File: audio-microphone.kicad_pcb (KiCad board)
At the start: 2 copper layers, 11.2 x 11.5 mm, 9 parts, among them J1 JST_SUR_1x5_BM05B-SURS-TB-LF-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

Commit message: [#71550] Change PCB to 4 layers
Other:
- copper layers 2 -> 4
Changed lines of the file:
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@@
 	(layers
 		(0 "F.Cu" signal)
+		(1 "In1.Cu" signal)
+		(2 "In2.Cu" signal)
 		(31 "B.Cu" signal)
 		(32 "B.Adhes" user "B.Adhesive")
@@
 			)
 			(layer "dielectric 1"
-				(type "core")
+				(type "prepreg")
 				(color "Polyimide")
-				(thickness 1.51)
+				(thickness 0.1)
 				(material "FR4")
 				(epsilon_r 4.5)
+				(loss_tangent 0.02)
+			)
+			(layer "In1.Cu"
+				(type "copper")
+				(thickness 0.035)
+			)
+			(layer "dielectric 2"
+				(type "core")
+				(thickness 1.24)
+				(material "FR4")
+				(epsilon_r 4.5)
+				(loss_tangent 0.02)
+			)
+			(layer "In2.Cu"
+				(type "copper")
+				(thickness 0.035)
+			)
+			(layer "dielectric 3"
+				(type "prepreg")
+				(thickness 0.1)
+				(material "FR4")
+				(epsilon_r 4.5)

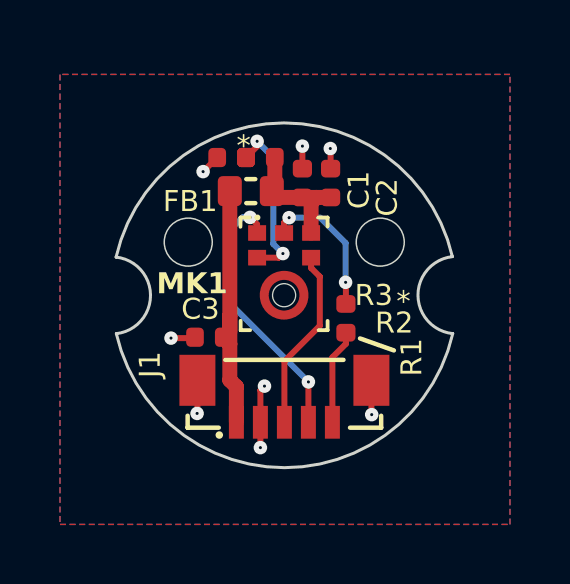
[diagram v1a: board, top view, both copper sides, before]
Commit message: [#71550] Change FB1 to 0402 size one BLM15AG601SN1D
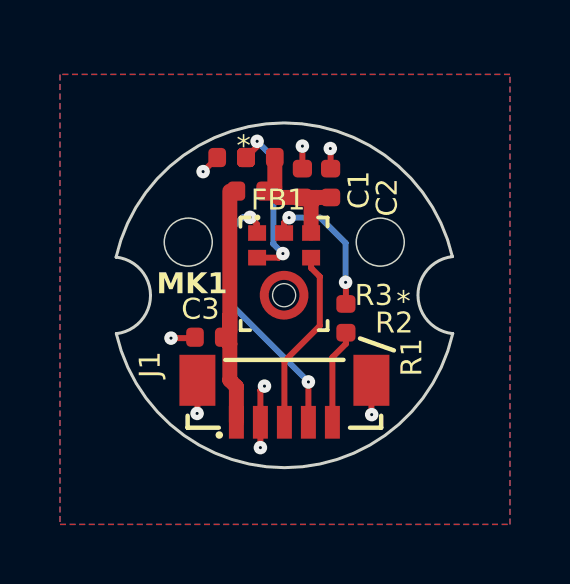
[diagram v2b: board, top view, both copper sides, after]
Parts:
- FB1: value FB_600Z_0.5A_Murata-BLM18AG_0603 -> FB_600Z_0.3A_Murata-BLM15AG_0402; footprint antmicro-footprints:FB_0603_1608Metric -> antmicro-footprints:FB_0402_1005Metric

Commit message: [#71550] Re-arrange components, finish routing
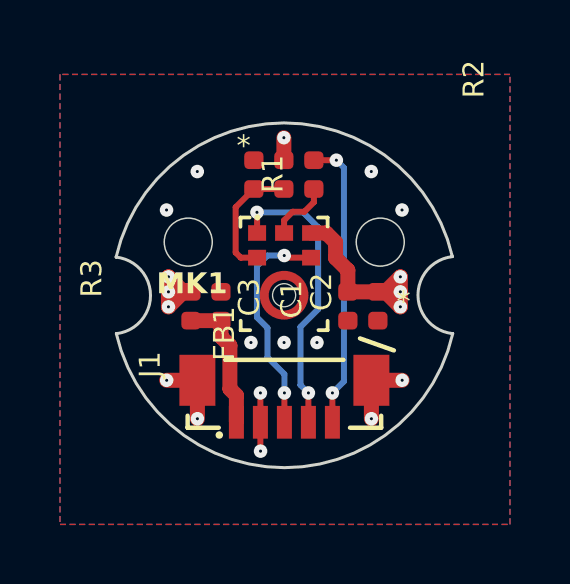
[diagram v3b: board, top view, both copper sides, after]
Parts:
- moved R1 4.91 mm to (241.0, 142.9), turned to 90 degrees
- moved C2 4.40 mm to (243.1, 147.3), turned to -90 degrees
- moved C1 4.38 mm to (242.1, 147.3), turned to 90 degrees
- moved FB1 4.32 mm to (236.9, 147.3), turned to -90 degrees
- moved C3 1.10 mm to (237.9, 147.3), turned to -90 degrees
- moved R2 0.97 mm to (240.0, 142.9), turned to 90 degrees
- moved R3 0.94 mm to (239.0, 142.9), turned to -90 degrees
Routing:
- net VDD: track 4.47 -> 11.3 mm, vias 0 -> 7
- net /DATA: track 3.17 -> 9.75 mm, vias 0 -> 2
- net VCC: track 8.62 -> 4.60 mm
- net Net-(MK1-DATA): track 4.85 -> 2.11 mm, vias 2 -> 0
- net /SELECT: track 5.71 -> 4.16 mm, vias 2 -> 0
- net /BCLK: track 6.10 -> 7.57 mm, vias 0 -> 2
- net /WS: track 9.00 -> 9.79 mm
- net GND: track 7.25 -> 6.56 mm, vias 8 -> 13
- added copper zone on In1.Cu, net GND
- added copper zone on In2.Cu, net VDD

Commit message: [#71550] Remove unnecessary vias
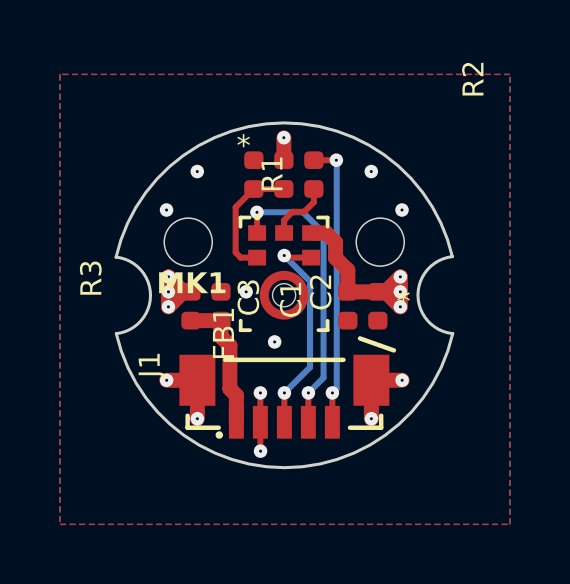
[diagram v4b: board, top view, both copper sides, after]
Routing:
- net GND: vias 13 -> 12
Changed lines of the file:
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@@
 	)
 	(via
-		(at 239.97 148.497305)
+		(at 239.655108 148.477305)
 		(size 0.45)
 		(drill 0.1)
@@
 	)
 	(via
-		(at 241.065108 148.497305)
-		(size 0.45)
-		(drill 0.1)
-		(layers "F.Cu" "B.Cu")
-		(net 2)
-	)
-	(via
 		(at 237.08 151.037305)
 		(size 0.45)
@@
 	)
 	(via
-		(at 238.865108 148.497305)
-		(size 0.45)
-		(drill 0.1)
-		(layers "F.Cu" "B.Cu")
-		(net 2)
-	)
-	(via
 		(at 242.876194 142.79752)
+		(size 0.45)
+		(drill 0.1)
+		(layers "F.Cu" "B.Cu")
+		(net 2)
+	)
+	(via
+		(at 238.705108 146.807305)
 		(size 0.45)
 		(drill 0.1)
@@
 	)
 	(segment
+		(start 241.285108 144.837305)
+		(end 241.285108 149.672197)
+		(width 0.2)
+		(layer "B.Cu")
+		(net 4)
+	)
+	(segment
 		(start 240.605108 144.157305)
-		(end 239.065108 144.157305)
-		(width 0.2)
-		(layer "B.Cu")
-		(net 4)
-	)
-	(segment
-		(start 240.515108 149.912413)
-		(end 240.515108 147.977305)
-		(width 0.2)
-		(layer "B.Cu")
-		(net 4)
-	)
-	(segment
-		(start 240.78 150.177305)
-		(end 240.515108 149.912413)
-		(width 0.2)
-		(layer "B.Cu")
-		(net 4)
-	)
-	(segment
-		(start 241.105108 147.387305)
-		(end 241.105108 144.657305)
-		(width 0.2)
-		(layer "B.Cu")
-		(net 4)
-	)
-	(segment
-		(start 241.105108 144.657305)
+		(end 241.285108 144.837305)
+		(width 0.2)
+		(layer "B.Cu")
+		(net 4)
+	)
+	(segment
+		(start 239.065108 144.157305)
 		(end 240.605108 144.157305)
 		(width 0.2)
@@
 	)
 	(segment
-		(start 240.515108 147.977305)
-		(end 241.105108 147.387305)
+		(start 241.285108 149.672197)
+		(end 240.78 150.177305)
 		(width 0.2)
 		(layer "B.Cu")
@@
 	)
 	(segment
-		(start 241.965108 149.792197)
-		(end 241.965108 142.672305)
+		(start 241.725108 150.032197)
+		(end 241.725108 142.432305)
 		(width 0.2)
 		(layer "B.Cu")
@@
 	(segment
 		(start 241.58 150.177305)
-		(end 241.965108 149.792197)
-		(width 0.2)
-		(layer "B.Cu")
-		(net 5)
-	)
-	(segment
-		(start 241.965108 142.672305)
+		(end 241.725108 150.032197)
+		(width 0.2)
+		(layer "B.Cu")
+		(net 5)
+	)
+	(segment
+		(start 241.725108 142.432305)
 		(end 241.712108 142.419305)
 		(width 0.2)
@@
 	)
 	(segment
-		(start 239.065108 145.947305)
-		(end 239.415108 145.597305)
-		(width 0.2)
-		(layer "B.Cu")
-		(net 6)
-	)
-	(segment
-		(start 239.415108 148.987305)
-		(end 239.415108 148.007305)
-		(width 0.2)
-		(layer "B.Cu")
-		(net 6)
-	)
-	(segment
-		(start 239.415108 148.007305)
-		(end 239.065108 147.657305)
-		(width 0.2)
-		(layer "B.Cu")
-		(net 6)
-	)
-	(segment
-		(start 239.065108 147.657305)
-		(end 239.065108 145.947305)
-		(width 0.2)
-		(layer "B.Cu")
-		(net 6)
-	)
-	(segment
-		(start 239.98 150.177305)
-		(end 239.98 149.552197)
-		(width 0.2)
-		(layer "B.Cu")
-		(net 6)
-	)
-	(segment
-		(start 239.415108 145.597305)
-		(end 239.975108 145.597305)
-		(width 0.2)
-		(layer "B.Cu")
-		(net 6)
-	)
-	(segment
-		(start 239.98 149.552197)
-		(end 239.415108 148.987305)
-		(width 0.2)
-		(layer "B.Cu")
+		(start 240.835108 146.457305)
+		(end 240.835108 149.322197)
+		(width 0.2)
+		(layer "B.Cu")
+		(net 6)
+	)
+	(segment
+		(start 240.835108 149.322197)
+		(end 239.98 150.177305)
+		(width 0.2)
+		(layer "B.Cu")
+		(net 6)
+	)
+	(segment
+		(start 239.975108 145.597305)
+		(end 240.835108 146.457305)
+		(width 0.2)
+		(layer "B.Cu")

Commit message: [#71550] Limit board size to 11 mm in diameter, clear DRC
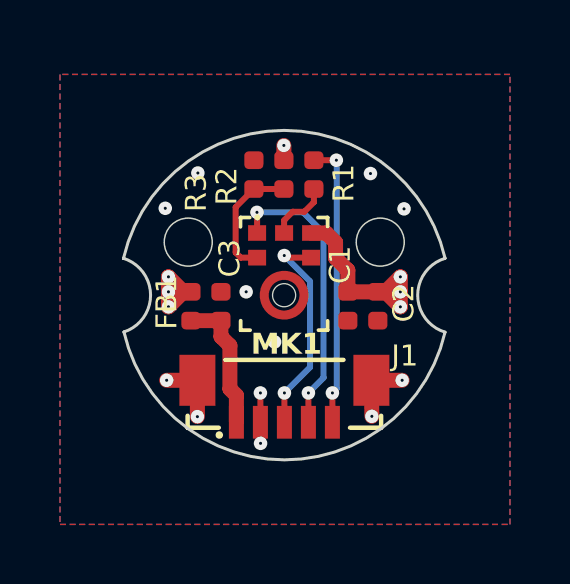
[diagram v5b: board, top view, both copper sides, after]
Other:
- board size 11.2 x 11.5 mm -> 10.7 x 11 mm
- board text removed: "*"
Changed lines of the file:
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@@
 		(tags "capacitor SMD 0402")
 		(property "Reference" "C2"
-			(at -1.12 2.29 90)
+			(at -0.74 -0.45 90)
 			(layer "F.SilkS")
 			(effects
@@
 		(tags "ferrite bead SMD 0402")
 		(property "Reference" "FB1"
-			(at 0 -0.7 90)
+			(at -1.04 1.22 90)
 			(layer "F.SilkS")
 			(effects
@@
 		(tags "capacitor SMD 0402")
 		(property "Reference" "C1"
-			(at -0.41 -1.47 90)
+			(at 0.74 0.15 90)
 			(layer "F.SilkS")
 			(effects
@@
 		(tags "capacitor SMD 0402")
 		(property "Reference" "C3"
-			(at -0.94 -0.53 90)
+			(at -2.24 0.12 90)
 			(layer "F.SilkS")
 			(effects
@@
 		(tags "resistor SMD 0402")
 		(property "Reference" "R3"
-			(at 4.1 5 90)
+			(at 1.248 1.517 90)
 			(layer "F.SilkS")
 			(effects
@@
 		(at 239.98 150.2 90)
 		(property "Reference" "J1"
-			(at 0.52 -4.07 90)
+			(at 0.852695 3.565108 0)
 			(unlocked yes)
 			(layer "F.SilkS")
@@
 		(descr "Footprint based on: https://eu.mouser.com/datasheet/2/218/ph0645lm4h_b_datasheet_rev_c-1525723.pdf")
 		(property "Reference" "MK1"
-			(at -3.07 -0.39 0)
+			(at 0.075108 1.627305 0)
 			(layer "F.SilkS")
 			(effects
@@
 		(tags "resistor SMD 0402")
 		(property "Reference" "R1"
-			(at 0.66 -1.78 90)
+			(at 0.352 0.583 90)
 			(layer "F.SilkS")
 			(effects
@@
 		(tags "resistor SMD 0402")
 		(property "Reference" "R2"
-			(at 3.82 5.92 90)
+			(at 0.252 -2.317 90)
 			(layer "F.SilkS")
 			(effects
@@
 	)
 	(gr_line
-		(start 243.63 148.76)
-		(end 242.5 148.36)
-		(stroke
-			(width 0.15)
-			(type default)
-		)
-		(layer "F.SilkS")
-	)
-	(gr_line
 		(start 239.975 134.8)
 		(end 239.975 160.45)
@@
 		(layer "Dwgs.User")
 	)
+	(gr_arc
+		(start 235.514004 143.219066)
+		(mid 235.845108 144.547305)
+		(end 234.539312 144.958089)
+		(stroke
+			(width 0.15)
+			(type default)
+		)
+		(layer "Dwgs.User")
+	)
 	(gr_line
 		(start 227.875001 146.925)
@@
 	)
 	(gr_arc
-		(start 235.58 143.19)
-		(mid 235.867471 144.516255)
-		(end 234.571351 144.918328)
+		(start 245.335581 148.1515)
+		(mid 244.422867 146.919999)
+		(end 245.336361 145.689077)
 		(stroke
-			(width 0.15)
+			(width 0.1)
 			(type default)
 		)
-		(layer "Dwgs.User")
+		(layer "Edge.Cuts")
 	)
 	(gr_arc
-		(start 245.59 148.199999)
-		(mid 244.432261 146.921531)
-		(end 245.579299 145.633453)
+		(start 234.616 145.689729)
+		(mid 235.519346 146.911695)
+		(end 234.631038 148.144636)
 		(stroke
 			(width 0.1)
@@
 	)
 	(gr_line
-		(start 245.591228 148.201616)
-		(end 245.589611 148.199999)
+		(start 234.615579 145.69107)
+		(end 234.616 145.689729)
 		(stroke
 			(width 0.1)
@@
 	)
 	(gr_arc
-		(start 234.369239 145.650538)
-		(mid 239.967463 141.176258)
-		(end 245.579299 145.633453)
-		(stroke
-			(width 0.1)
-			(type default)
-		)
-		(layer "Edge.Cuts")
-	)
-	(gr_arc
-		(start 234.369239 145.650538)
-		(mid 235.517134 146.92256)
-		(end 234.376895 148.201372)
+		(start 234.615579 145.69107)
+		(mid 239.975177 141.425437)
+		(end 245.336361 145.689076)
 		(stroke
 			(width 0.1)
@@
 	)
 	(gr_arc
-		(start 245.591228 148.201616)
-		(mid 239.983963 152.668734)
-		(end 234.376895 148.201372)
+		(start 245.335581 148.151502)
+		(mid 239.980577 152.408327)
+		(end 234.631038 148.144636)
 		(stroke
 			(width 0.1)
@@
 	)
 	(gr_text "Audio\nMicrophone"
-		(at 239.95 151.61 0)
+		(at 239.95 151.037305 0)
 		(layer "B.SilkS")
 		(effects
@@
 	)
 	(gr_text "SHA:########"
-		(at 243.97 149.42 0)
+		(at 243.97 148.847305 0)
 		(layer "B.SilkS")
 		(effects
@@
 		)
 	)
-	(gr_text "*"
-		(at 238.38 142.35 0)
-		(layer "F.SilkS")
-		(effects
-			(font
-				(size 0.7 0.7)
-				(thickness 0.15)
-			)
-			(justify left bottom)
-		)
-	)
-	(gr_text "*"
-		(at 243.71 147.54 0)
-		(layer "F.SilkS")
-		(effects
-			(font
-				(size 0.7 0.7)
-				(thickness 0.15)
-			)
-			(justify left bottom)
-		)
-	)
 	(dimension
 		(type aligned)
 		(layer "Dwgs.User")
 		(pts
-			(xy 234.2329 146.9248) (xy 245.723 146.9161)
+			(xy 239.980577 152.408327) (xy 239.975177 141.425437)
 		)
-		(height 16.12251)
-		(gr_text "11,4901 mm"
-			(at 239.989287 161.892955 0.04338284145)
+		(height 14.190287)
+		(gr_text "10,9829 mm"
+			(at 255.318162 146.90934 -89.97182916)
 			(layer "Dwgs.User")
 			(effects
@@
 	)
 	(segment
+		(start 239.962108 142.419305)
+		(end 239.962108 141.926305)
+		(width 0.5)
+		(layer "F.Cu")
+		(net 1)
+	)
+	(segment
 		(start 236.115108 147.307305)
 		(end 236.115108 146.807305)
@@
 	)
 	(segment
-		(start 239.962108 142.419305)
-		(end 239.962108 141.669305)
-		(width 0.5)
-		(layer "F.Cu")
-		(net 1)
-	)
-	(segment
 		(start 243.095108 146.807305)
 		(end 243.345108 146.807305)
@@
 	)
 	(via
-		(at 239.962108 141.669305)
+		(at 239.962108 141.926305)
 		(size 0.45)
 		(drill 0.1)
@@
 	)
 	(segment
+		(start 239.18 151.852197)
+		(end 239.185108 151.857305)
+		(width 0.2)
+		(layer "F.Cu")
+		(net 2)
+	)
+	(segment
 		(start 237.08 149.755)
-		(end 237.08 151.037305)
+		(end 237.08 150.967305)
 		(width 0.5)
 		(layer "F.Cu")
@@
 	(segment
 		(start 239.18 151.155)
-		(end 239.18 152.112197)
+		(end 239.18 151.852197)
 		(width 0.2)
 		(layer "F.Cu")
@@
 	(segment
 		(start 242.88 149.755)
-		(end 242.88 151.037305)
+		(end 242.895108 150.957305)
 		(width 0.5)
 		(layer "F.Cu")
@@
 		(net 2)
 	)
-	(segment
-		(start 239.18 152.112197)
-		(end 239.185108 152.117305)
-		(width 0.2)
-		(layer "F.Cu")
-		(net 2)
-	)
 	(via
-		(at 237.076194 142.79752)
+		(at 237.095108 142.846305)
 		(size 0.45)
 		(drill 0.1)
@@
 	)
 	(via
-		(at 236.051302 144.079825)
+		(at 236.009108 144.022305)
 		(size 0.45)
 		(drill 0.1)
@@
 	)
 	(via
-		(at 242.88 151.037305)
+		(at 239.185108 151.857305)
 		(size 0.45)
 		(drill 0.1)
@@
 	)
 	(via
-		(at 237.08 151.037305)
+		(at 242.895108 150.957305)
 		(size 0.45)
 		(drill 0.1)
@@
 	)
 	(via
-		(at 242.876194 142.79752)
+		(at 237.08 150.967305)
 		(size 0.45)
 		(drill 0.1)
@@
 	)
 	(via
-		(at 238.705108 146.807305)
+		(at 242.849108 142.864305)
 		(size 0.45)
 		(drill 0.1)
@@
 	)
 	(via
-		(at 243.901086 144.079825)
+		(at 238.705108 146.807305)
 		(size 0.45)
 		(drill 0.1)
@@
 	)
 	(via
-		(at 239.18 150.177305)
+		(at 243.968108 144.041305)
 		(size 0.45)
 		(drill 0.1)
@@
 	)
 	(via
-		(at 239.185108 152.117305)
+		(at 239.18 150.177305)
 		(size 0.45)
 		(drill 0.1)
